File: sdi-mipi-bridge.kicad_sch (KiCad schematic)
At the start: 186 parts, among them J1 Conn_BNC_031-70526-21, J2 Conn_BNC_031-70526-21, J3 Conn_FFC_68715014522_ONE-SIDE, J4 PinHeader_2x5_P1.27mm_Vertical, J5 PinHeader_1x4_P1.27mm_Drill.7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, J6 PinHeader_2x5_P1.27mm_Vertical, U1 MAX8902B, U2 GS2971A, U3 GS2988, U4 CrossLink_LIF-MD6000-6JMG80I, U5 SC18IS602BIPW, Y1 Oscillator_SMD_27MHz_ABM7

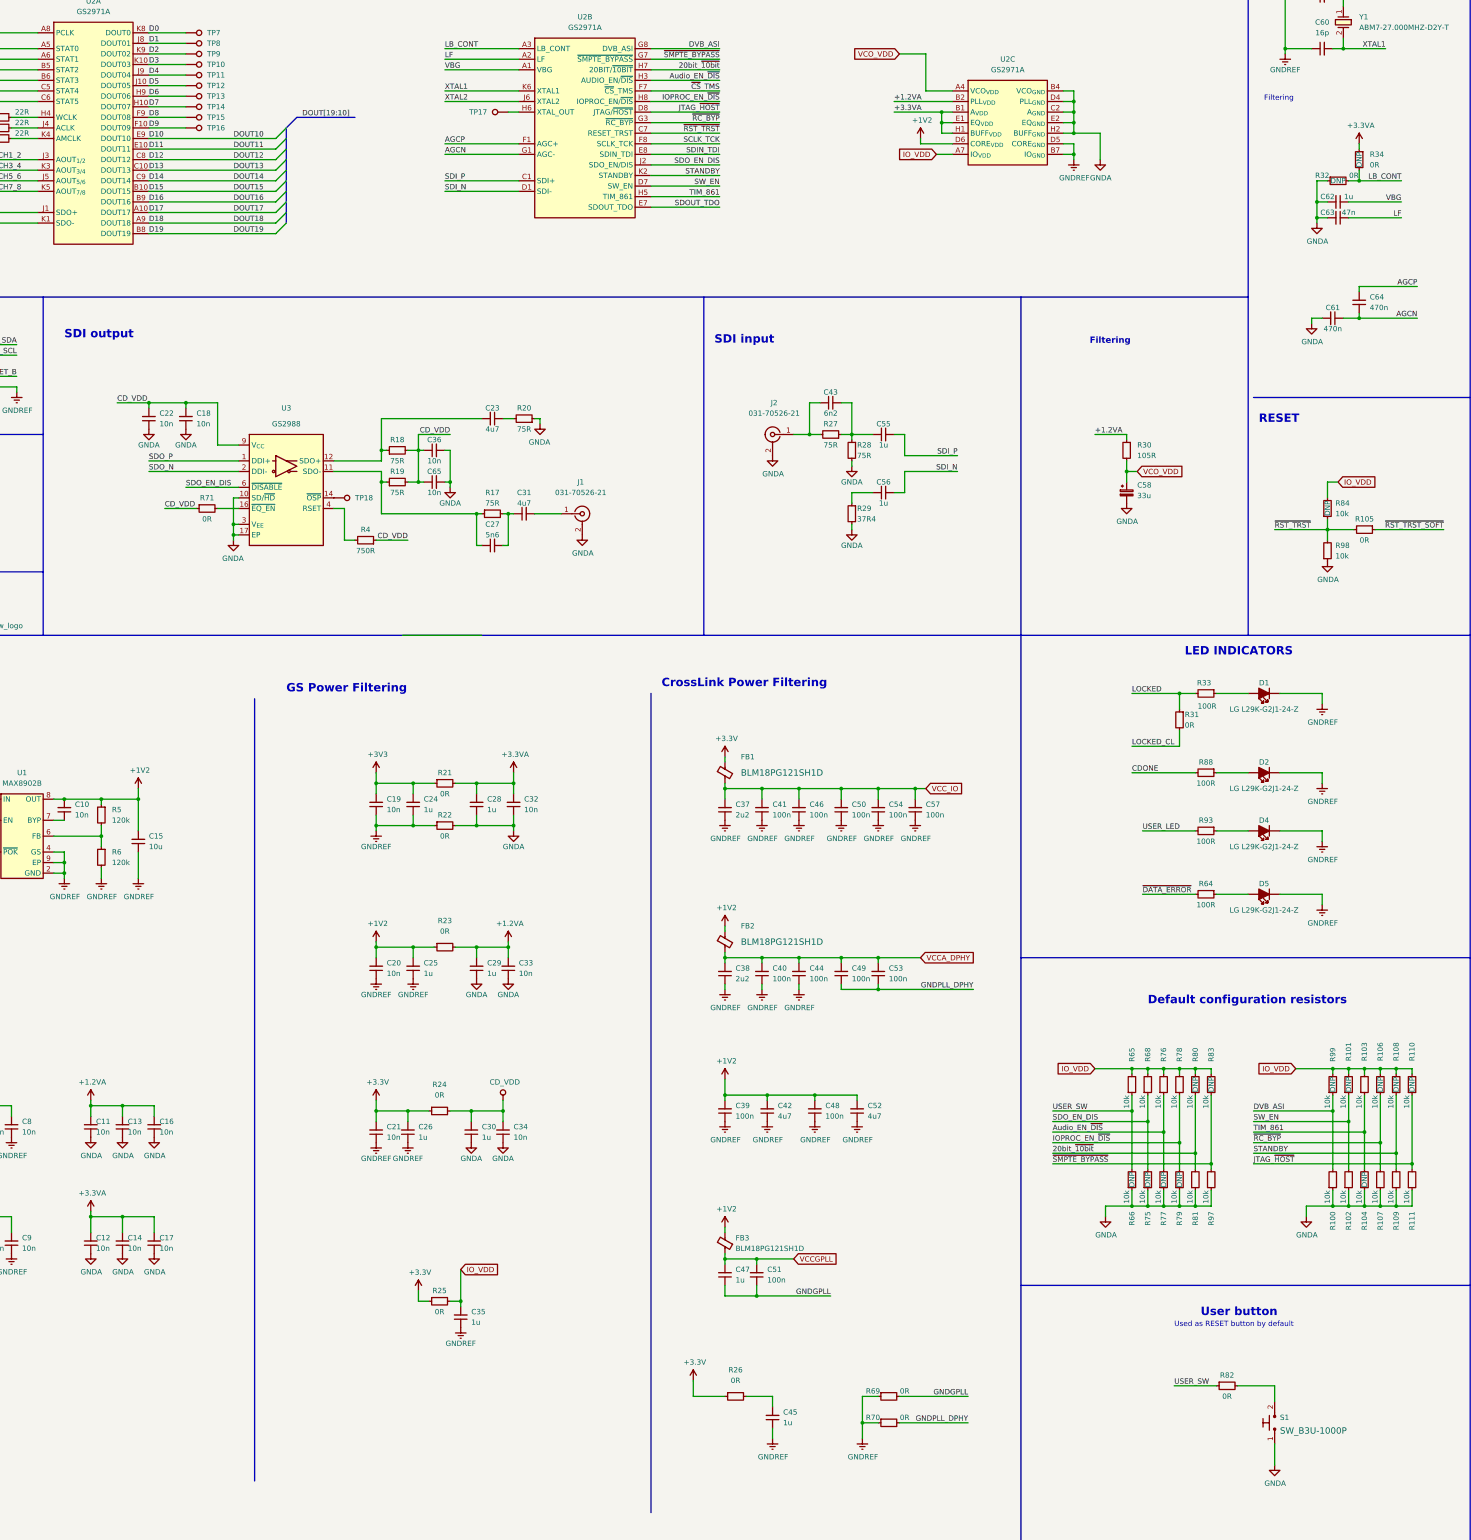
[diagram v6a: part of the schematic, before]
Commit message: Imported schematic changes to the PCB and placed components
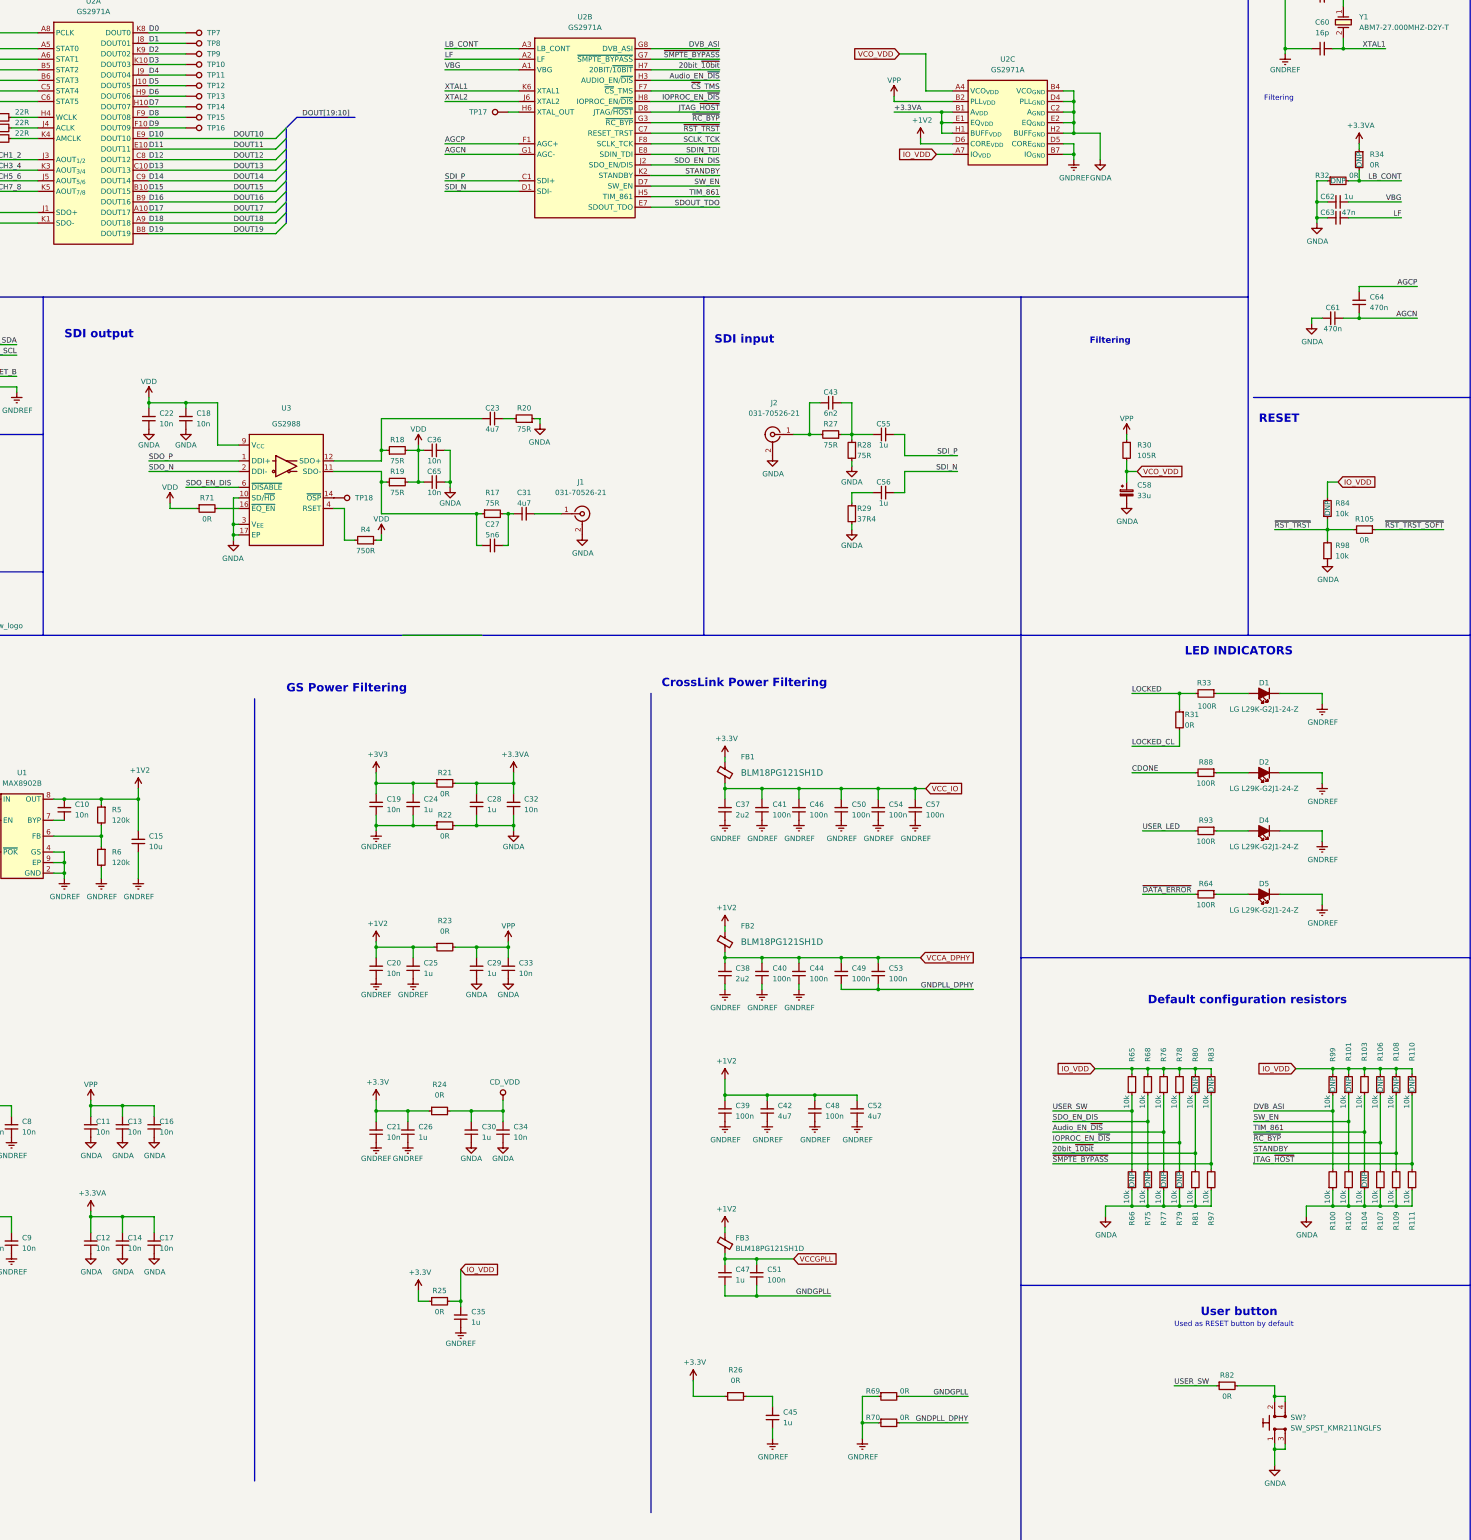
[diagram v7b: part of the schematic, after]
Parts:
- removed S1: SW_B3U-1000P, antmicro-footprints:SW_B3U-3000P, symbol antmicroTactileSwitches:SW_B3U-1000P
- added SW?: SW_SPST_KMR211NGLFS, antmicro-footprints:SW_SPST_4.2x2.8, symbol antmicroPushbuttonSwitches:SW_SPST_KMR211NGLFS
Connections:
- net +1.2VA is gone; now on net VPP: R30.1, U2.B2 (PLL_{VDD}), U2.C3 (PLL_{VDD}), U2.C4 (PLL_{VDD})
- net CD_VDD is gone; now on net VDD: C18.2, C22.2, C36.1, C65.1, R18.2, R19.2, R4.1, R71.1, U3.9 (V_{CC})
- net GNDA: now also SW?.1, SW?.3
- net at R82.2: now also SW?.2, SW?.4

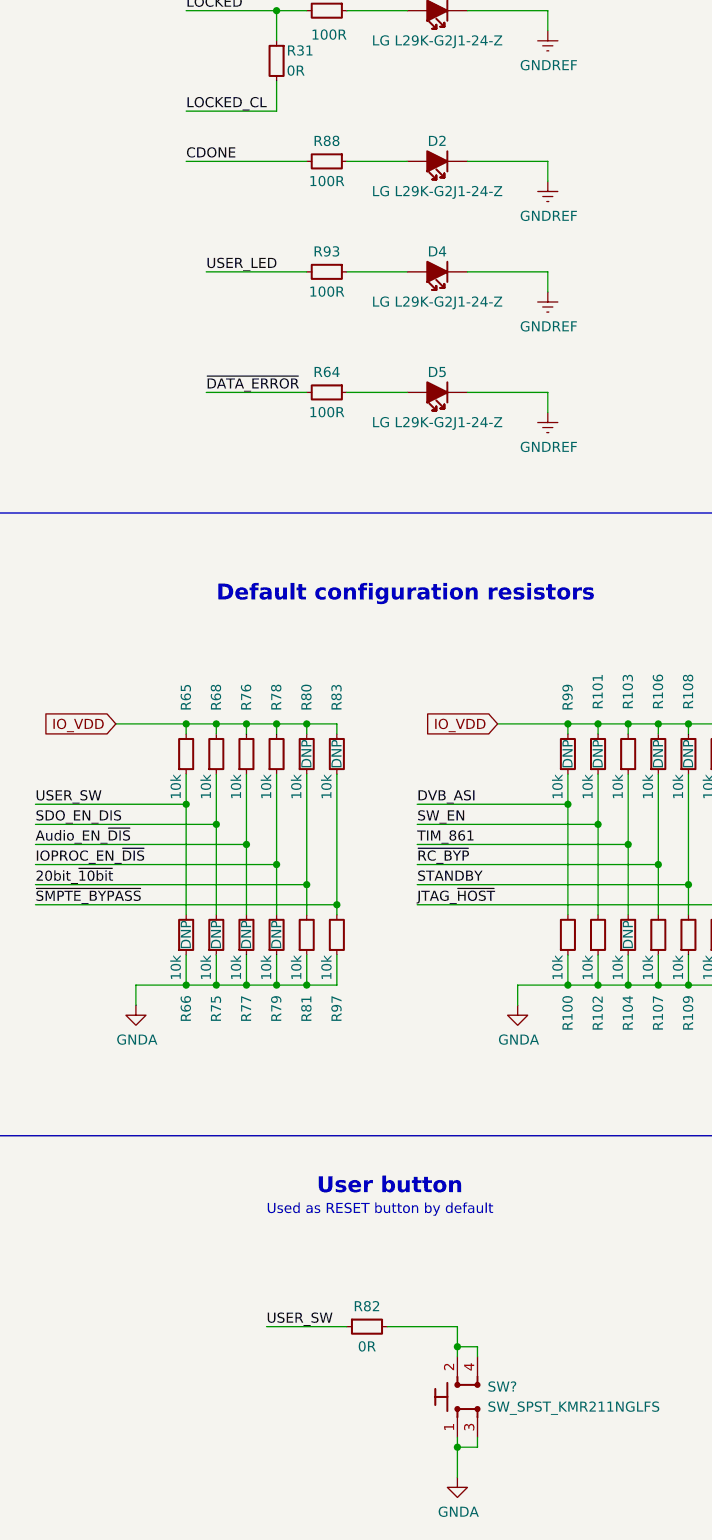
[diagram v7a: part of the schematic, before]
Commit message: Finished migrating the PCB silkscreen
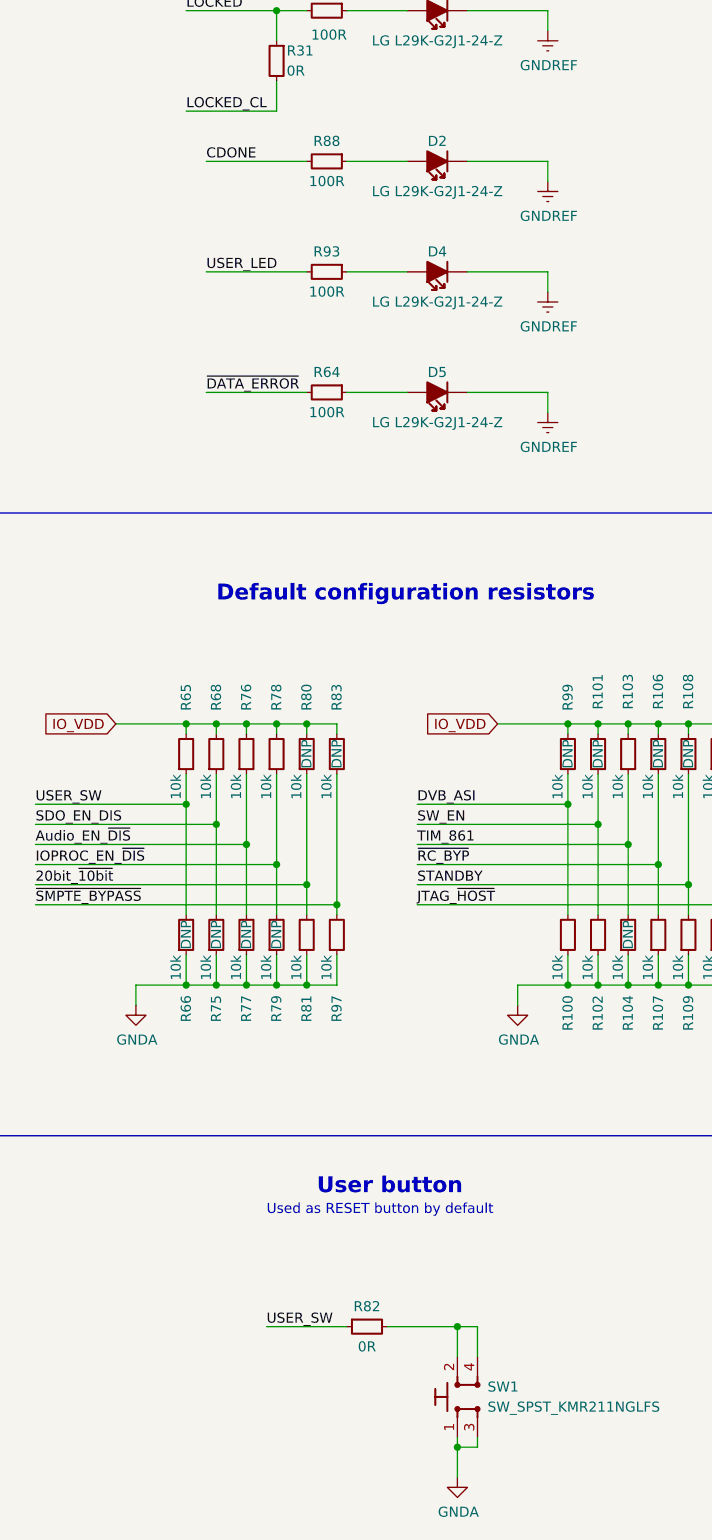
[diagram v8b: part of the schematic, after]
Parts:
- gave numbers to parts that had none: 1
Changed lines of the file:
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@@
   (junction (at 453.39 130.81) (diameter 0) (color 0 0 0 0)
   )
+  (junction (at 360.68 369.57) (diameter 0) (color 0 0 0 0)
+  )
   (junction (at 458.47 151.13) (diameter 0) (color 0 0 0 0)
   )
@@
   (junction (at 334.01 308.61) (diameter 0) (color 0 0 0 0)
   )
-  (junction (at 360.68 372.11) (diameter 0) (color 0 0 0 0)
-  )
   (junction (at 250.19 299.72) (diameter 0) (color 0 0 0 0)
   )
@@
     (stroke (width 0) (type default) (color 0 0 0 0))
   )
-  (wire (pts (xy 360.68 372.11) (xy 363.22 372.11))
+  (wire (pts (xy 360.68 369.57) (xy 363.22 369.57))
     (stroke (width 0) (type default) (color 0 0 0 0))
   )
@@
     (stroke (width 0) (type default) (color 0 0 0 0))
   )
-  (wire (pts (xy 326.39 222.25) (xy 341.63 222.25))
+  (wire (pts (xy 328.93 222.25) (xy 341.63 222.25))
     (stroke (width 0) (type default) (color 0 0 0 0))
   )
@@
     (stroke (width 0) (type default) (color 0 0 0 0))
   )
-  (wire (pts (xy 360.68 369.57) (xy 360.68 372.11))
-    (stroke (width 0) (type default) (color 0 0 0 0))
-  )
   (wire (pts (xy 368.3 326.39) (xy 368.3 328.93))
     (stroke (width 0) (type default) (color 0 0 0 0))
@@
     (stroke (width 0) (type default) (color 0 0 0 0))
   )
-  (wire (pts (xy 363.22 373.38) (xy 363.22 372.11))
+  (wire (pts (xy 363.22 373.38) (xy 363.22 369.57))
     (stroke (width 0) (type default) (color 0 0 0 0))
   )
@@
     (stroke (width 0) (type default) (color 0 0 0 0))
   )
-  (wire (pts (xy 360.68 372.11) (xy 360.68 373.38))
-    (stroke (width 0) (type default) (color 0 0 0 0))
-  )
   (wire (pts (xy 91.44 302.26) (xy 83.82 302.26))
     (stroke (width 0) (type default) (color 0 0 0 0))
@@
     (stroke (width 0) (type default) (color 0 0 0 0))
   )
+  (wire (pts (xy 360.68 369.57) (xy 360.68 373.38))
+    (stroke (width 0) (type default) (color 0 0 0 0))
+  )
   (wire (pts (xy 237.49 226.06) (xy 246.38 226.06))
     (stroke (width 0) (type default) (color 0 0 0 0))
@@
     (effects (font (size 1.27 1.27)) (justify left bottom))
   )
-  (label "CDONE" (at 326.39 222.25 0)
+  (label "CDONE" (at 328.93 222.25 0)
     (effects (font (size 1.27 1.27)) (justify left bottom))
   )
@@
   (symbol (lib_id "antmicroPushbuttonSwitches:SW_SPST_KMR211NGLFS") (at 360.68 383.54 90) (unit 1)
     (in_bom yes) (on_board yes) (fields_autoplaced)
-    (property "Reference" "SW?" (id 0) (at 364.49 377.1899 90)
+    (property "Reference" "SW1" (id 0) (at 364.49 377.1899 90)
       (effects (font (size 1.27 1.27) (thickness 0.15)) (justify right))
     )
@@
     )
     (path "/4d1cac73-7cdc-4785-ae72-51a7baf6dfb1"
-      (reference "SW?") (unit 1) (value "SW_SPST_KMR211NGLFS") (footprint "antmicro-footprints:SW_SPST_4.2x2.8")
+      (reference "SW1") (unit 1) (value "SW_SPST_KMR211NGLFS") (footprint "antmicro-footprints:SW_SPST_4.2x2.8")
     )
     (path "/00000000-0000-0000-0000-00005de76af8"
